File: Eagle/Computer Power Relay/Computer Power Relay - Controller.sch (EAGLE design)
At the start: 38 parts, among them U1 RP2040, U2 AP2112M-3.3TRG1

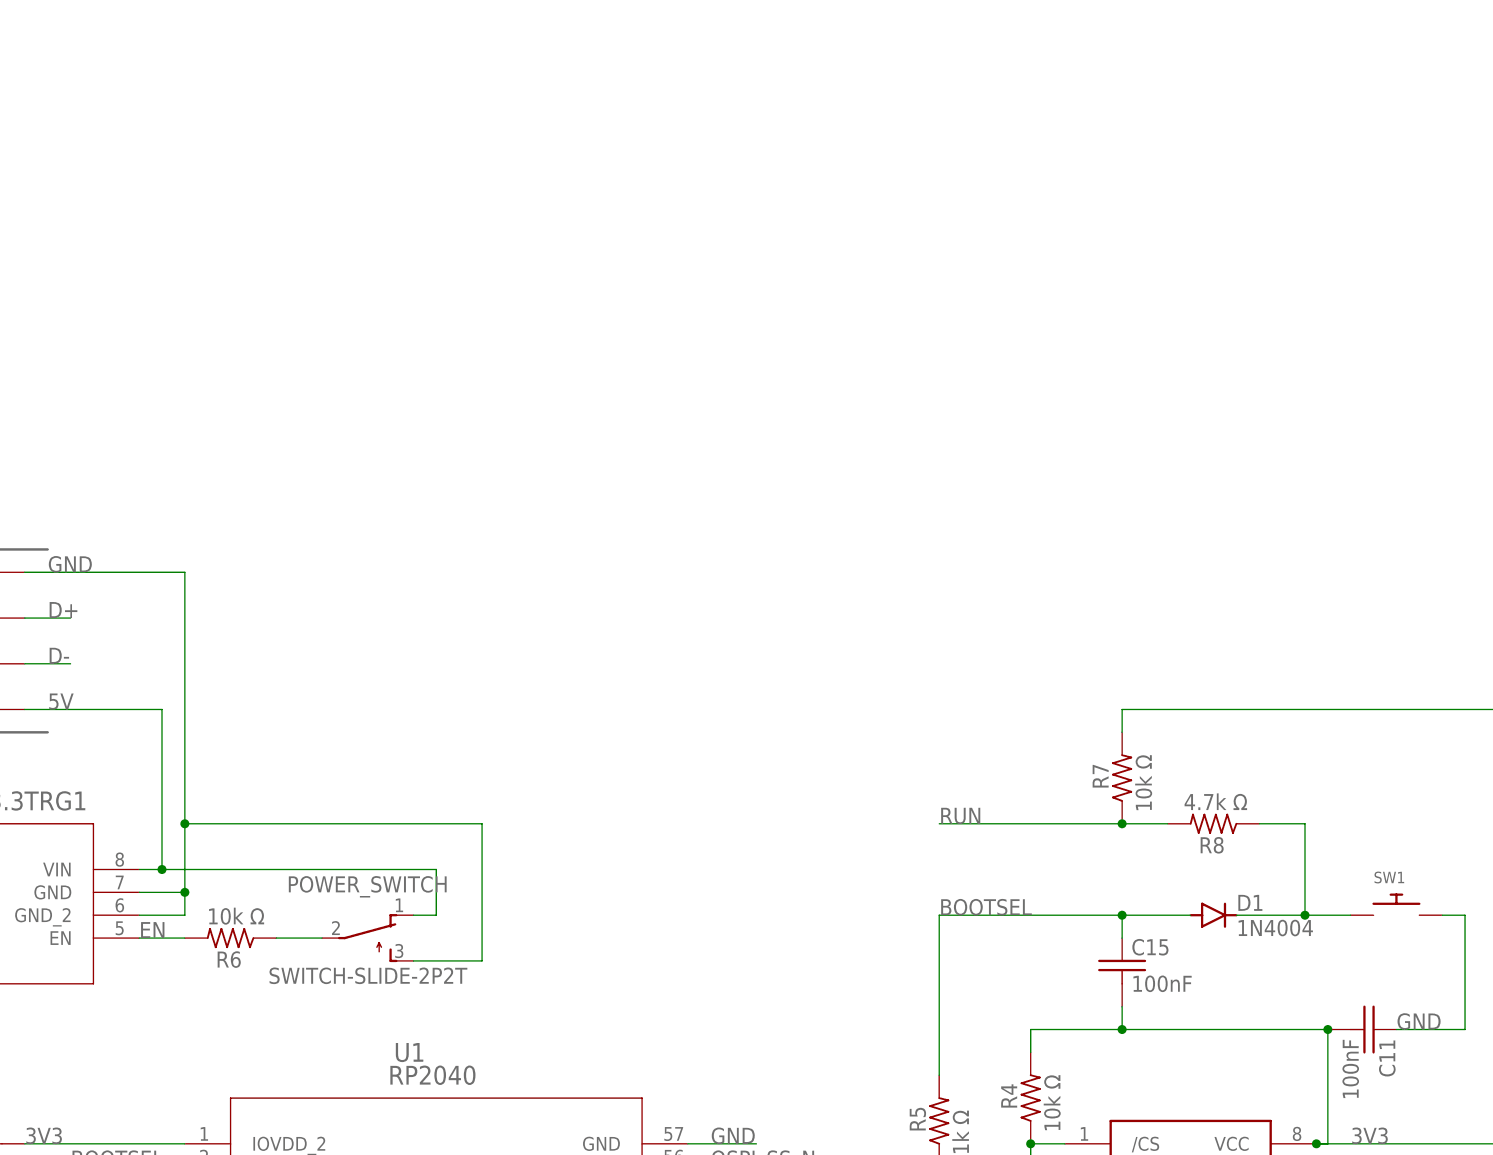
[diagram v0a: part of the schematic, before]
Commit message: Split controller from power splitter
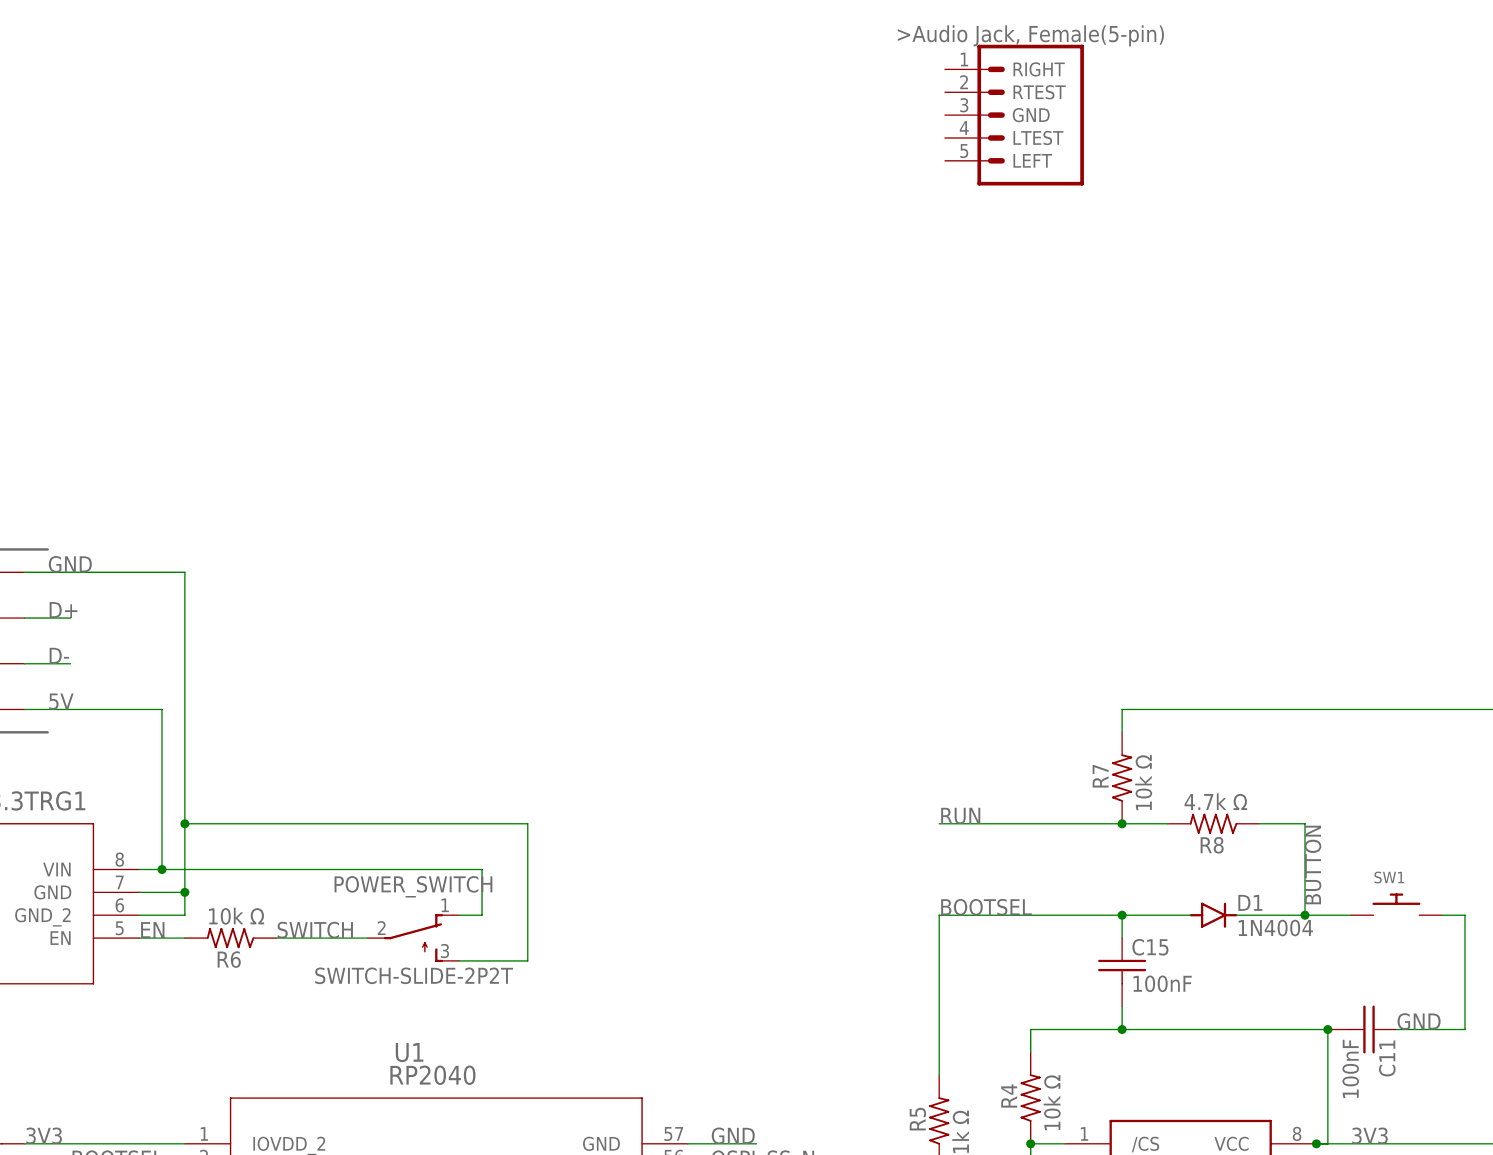
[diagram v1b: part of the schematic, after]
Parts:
- added U$3: AUDIO_JACK_FEMALE_5-PIN, Inventory:AUDIO_JACK_FEMALE_5-PIN
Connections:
- net N$7 renamed SWITCH
- net N$8 renamed BUTTON
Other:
- moved on the sheet: POWER_SWITCH
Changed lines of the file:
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@@
 <part name="R9" library="rcl" library_urn="urn:adsk.eagle:library:334" deviceset="R-US_" device="R0603" package3d_urn="urn:adsk.eagle:package:23555/3" value="27.4 Ω"/>
 <part name="R10" library="rcl" library_urn="urn:adsk.eagle:library:334" deviceset="R-US_" device="R0603" package3d_urn="urn:adsk.eagle:package:23555/3" value="27.4 Ω"/>
+<part name="U$3" library="Inventory" deviceset="AUDIO_JACK_FEMALE_5-PIN" device=""/>
 </parts>
 <sheets>
@@
 <attribute name="NAME" x="-30.48" y="67.818" size="1.778" layer="95" rot="R180" align="bottom-center"/>
 </instance>
-<instance part="POWER_SWITCH" gate="BEF1" x="53.34" y="104.14" smashed="yes" rot="R270">
-<attribute name="NAME" x="53.34" y="109.22" size="1.778" layer="95" align="bottom-center"/>
-<attribute name="VALUE" x="53.34" y="99.06" size="1.778" layer="96" align="bottom-center"/>
+<instance part="POWER_SWITCH" gate="BEF1" x="58.42" y="104.14" smashed="yes" rot="R270">
+<attribute name="NAME" x="58.42" y="109.22" size="1.778" layer="95" align="bottom-center"/>
+<attribute name="VALUE" x="58.42" y="99.06" size="1.778" layer="96" align="bottom-center"/>
 </instance>
 <instance part="R6" gate="G$1" x="38.1" y="104.14" smashed="yes" rot="R180">
@@
 <attribute name="VALUE" x="122.682" y="29.21" size="1.778" layer="96" rot="R90"/>
 </instance>
+<instance part="U$3" gate="G$1" x="127" y="195.58" smashed="yes"/>
 </instances>
 <busses>
@@
 <label x="17.78" y="144.78" size="1.778" layer="95"/>
 <pinref part="POWER_SWITCH" gate="BEF1" pin="S"/>
-<wire x1="58.42" y1="101.6" x2="66.04" y2="101.6" width="0.1524" layer="91"/>
-<wire x1="66.04" y1="101.6" x2="66.04" y2="116.84" width="0.1524" layer="91"/>
-<wire x1="66.04" y1="116.84" x2="33.02" y2="116.84" width="0.1524" layer="91"/>
+<wire x1="63.5" y1="101.6" x2="71.12" y2="101.6" width="0.1524" layer="91"/>
+<wire x1="71.12" y1="101.6" x2="71.12" y2="116.84" width="0.1524" layer="91"/>
+<wire x1="71.12" y1="116.84" x2="33.02" y2="116.84" width="0.1524" layer="91"/>
 <junction x="33.02" y="116.84"/>
 </segment>
@@
 <label x="17.78" y="129.54" size="1.778" layer="95"/>
 <pinref part="POWER_SWITCH" gate="BEF1" pin="O"/>
-<wire x1="58.42" y1="106.68" x2="60.96" y2="106.68" width="0.1524" layer="91"/>
-<wire x1="60.96" y1="106.68" x2="60.96" y2="111.76" width="0.1524" layer="91"/>
-<wire x1="60.96" y1="111.76" x2="30.48" y2="111.76" width="0.1524" layer="91"/>
+<wire x1="63.5" y1="106.68" x2="66.04" y2="106.68" width="0.1524" layer="91"/>
+<wire x1="66.04" y1="106.68" x2="66.04" y2="111.76" width="0.1524" layer="91"/>
+<wire x1="66.04" y1="111.76" x2="30.48" y2="111.76" width="0.1524" layer="91"/>
 <junction x="30.48" y="111.76"/>
 </segment>
@@
 </segment>
 </net>
-<net name="N$7" class="0">
+<net name="SWITCH" class="0">
 <segment>
 <pinref part="R6" gate="G$1" pin="1"/>
 <pinref part="POWER_SWITCH" gate="BEF1" pin="P"/>
-<wire x1="43.18" y1="104.14" x2="48.26" y2="104.14" width="0.1524" layer="91"/>
-</segment>
-</net>
-<net name="N$8" class="0">
+<wire x1="43.18" y1="104.14" x2="53.34" y2="104.14" width="0.1524" layer="91"/>
+<label x="43.18" y="104.14" size="1.778" layer="95"/>
+</segment>
+</net>
+<net name="BUTTON" class="0">
 <segment>
 <pinref part="SW1" gate="G$1" pin="P$1"/>
@@
 <wire x1="149.86" y1="106.68" x2="157.48" y2="106.68" width="0.1524" layer="91"/>
 <pinref part="D1" gate="1" pin="C"/>
-</segment>
-</net>
+<label x="157.48" y="116.84" size="1.778" layer="95" rot="R270"/>
+</segment>
+</net>

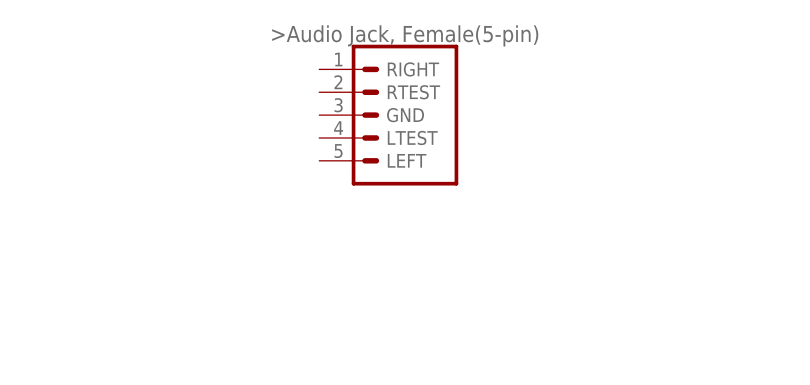
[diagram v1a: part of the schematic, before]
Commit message: Beginning Merge of Boards (Relay)
I'm beginning to merge the Controller and Power Strip boards into one so that I can print it for cheaper.
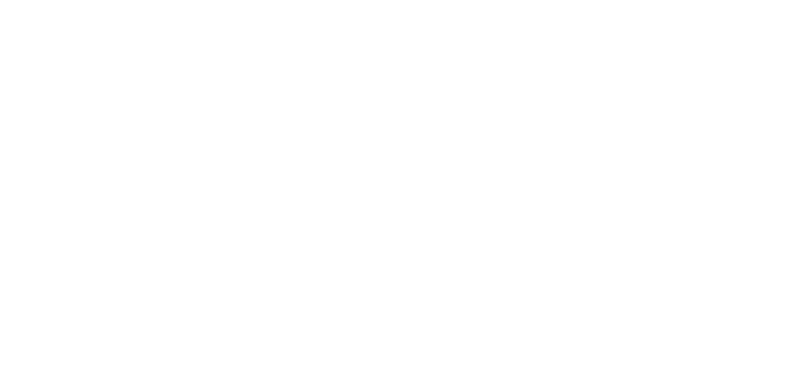
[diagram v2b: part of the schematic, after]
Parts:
- removed U$3: AUDIO_JACK_FEMALE_5-PIN, Inventory:AUDIO_JACK_FEMALE_5-PIN
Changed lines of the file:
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@@
 <part name="R9" library="rcl" library_urn="urn:adsk.eagle:library:334" deviceset="R-US_" device="R0603" package3d_urn="urn:adsk.eagle:package:23555/3" value="27.4 Ω"/>
 <part name="R10" library="rcl" library_urn="urn:adsk.eagle:library:334" deviceset="R-US_" device="R0603" package3d_urn="urn:adsk.eagle:package:23555/3" value="27.4 Ω"/>
-<part name="U$3" library="Inventory" deviceset="AUDIO_JACK_FEMALE_5-PIN" device=""/>
 </parts>
 <sheets>
@@
 <attribute name="VALUE" x="122.682" y="29.21" size="1.778" layer="96" rot="R90"/>
 </instance>
-<instance part="U$3" gate="G$1" x="127" y="195.58" smashed="yes"/>
 </instances>
 <busses>
